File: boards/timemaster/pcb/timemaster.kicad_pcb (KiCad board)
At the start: 6 copper layers, 37 x 35 mm, 59 parts, among them J1 Conn_02x03_Odd_Even, J2 Conn_Coaxial, J3 Conn_Coaxial, J4 Conn_Coaxial, J5 Conn_Coaxial, U1 SM05B-GHS-TB(LF)(SN), U2 SATA-401-M07S1BY-A, U3 STM32G031G8Ux, U4 SI5340B-D-GM, U5 TPS62231TDRYRQ1, X1 X2C048000L71H-CEHZ

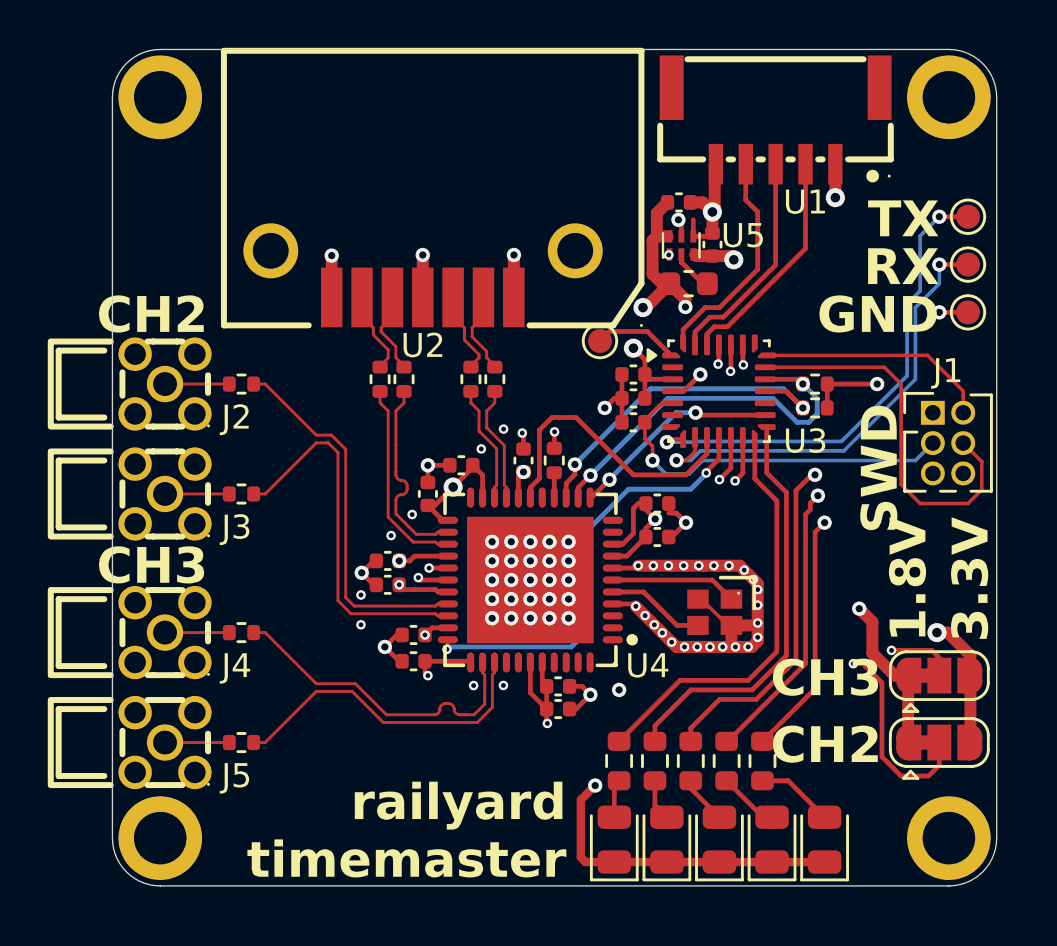
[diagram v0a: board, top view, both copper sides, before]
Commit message: timemaster: rev b with larger vias for jlc
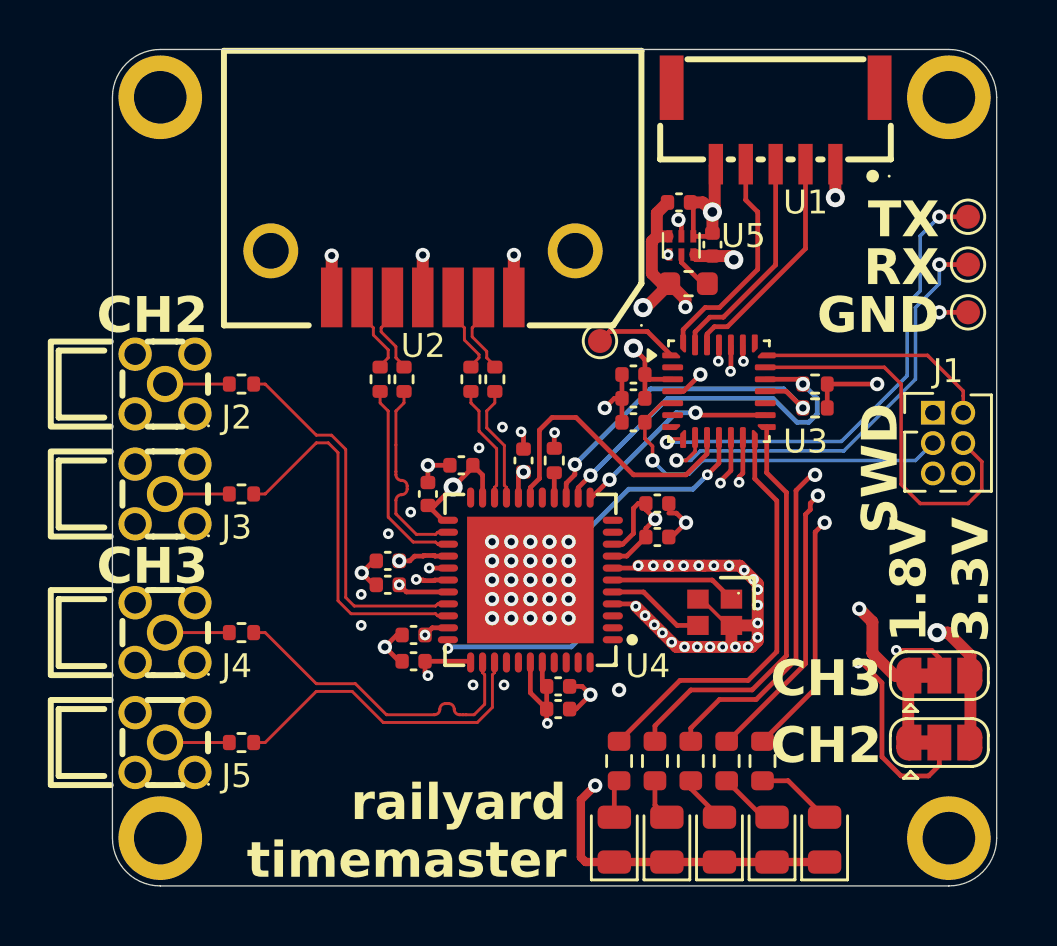
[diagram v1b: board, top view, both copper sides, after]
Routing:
- net GND: track 40.2 -> 41.1 mm
